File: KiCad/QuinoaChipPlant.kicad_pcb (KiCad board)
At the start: 2 copper layers, 22 x 97 mm, 26 parts, among them J1 POWER_SW, J2 POWER, J3 MOTOR, J4 SPEAKER, J5 NeoPixel, J6 Conn_01x04_Male, J8 Conn_01x04_Male, J9 Conn_01x01_Female, Q1 Q_NMOS_GSD, U1 SparkFun_TB6612FNG_MOTOR_DRIV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, U2 SparkFun_Pro_Micro_328U4, U3 MIC5205-3.3YM5, U4 TSPCBA-01-B2_nRF52810_module

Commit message: change to  KiCad 7 files from KiCad 5 files.
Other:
- net class Default removed

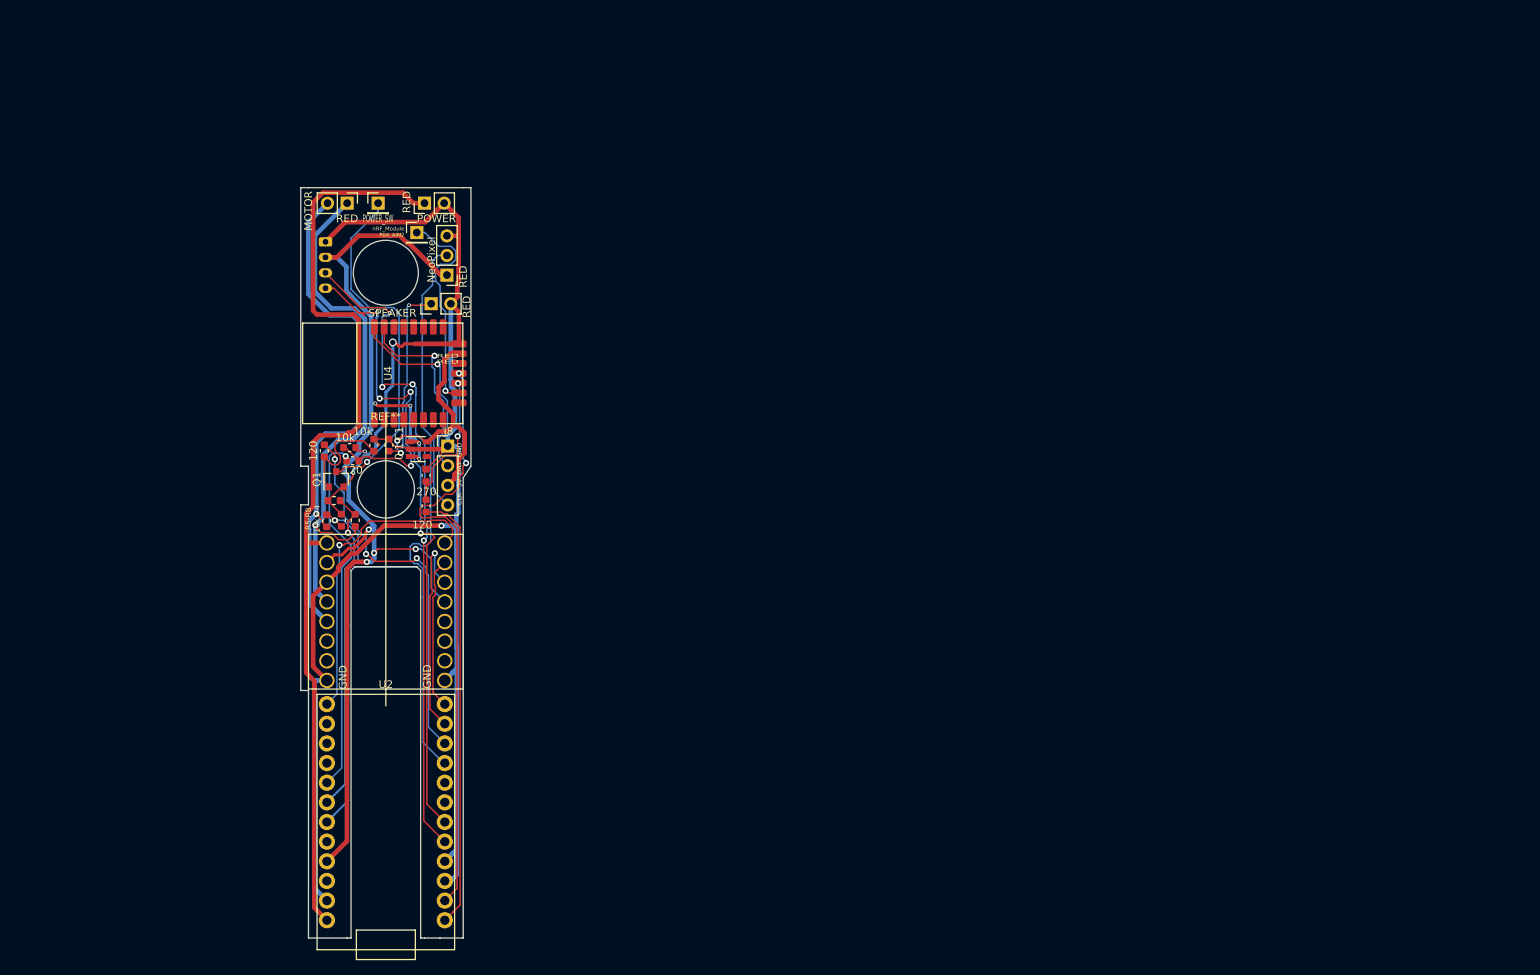
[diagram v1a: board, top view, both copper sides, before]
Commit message: make pump, bulb , sensor PCB.
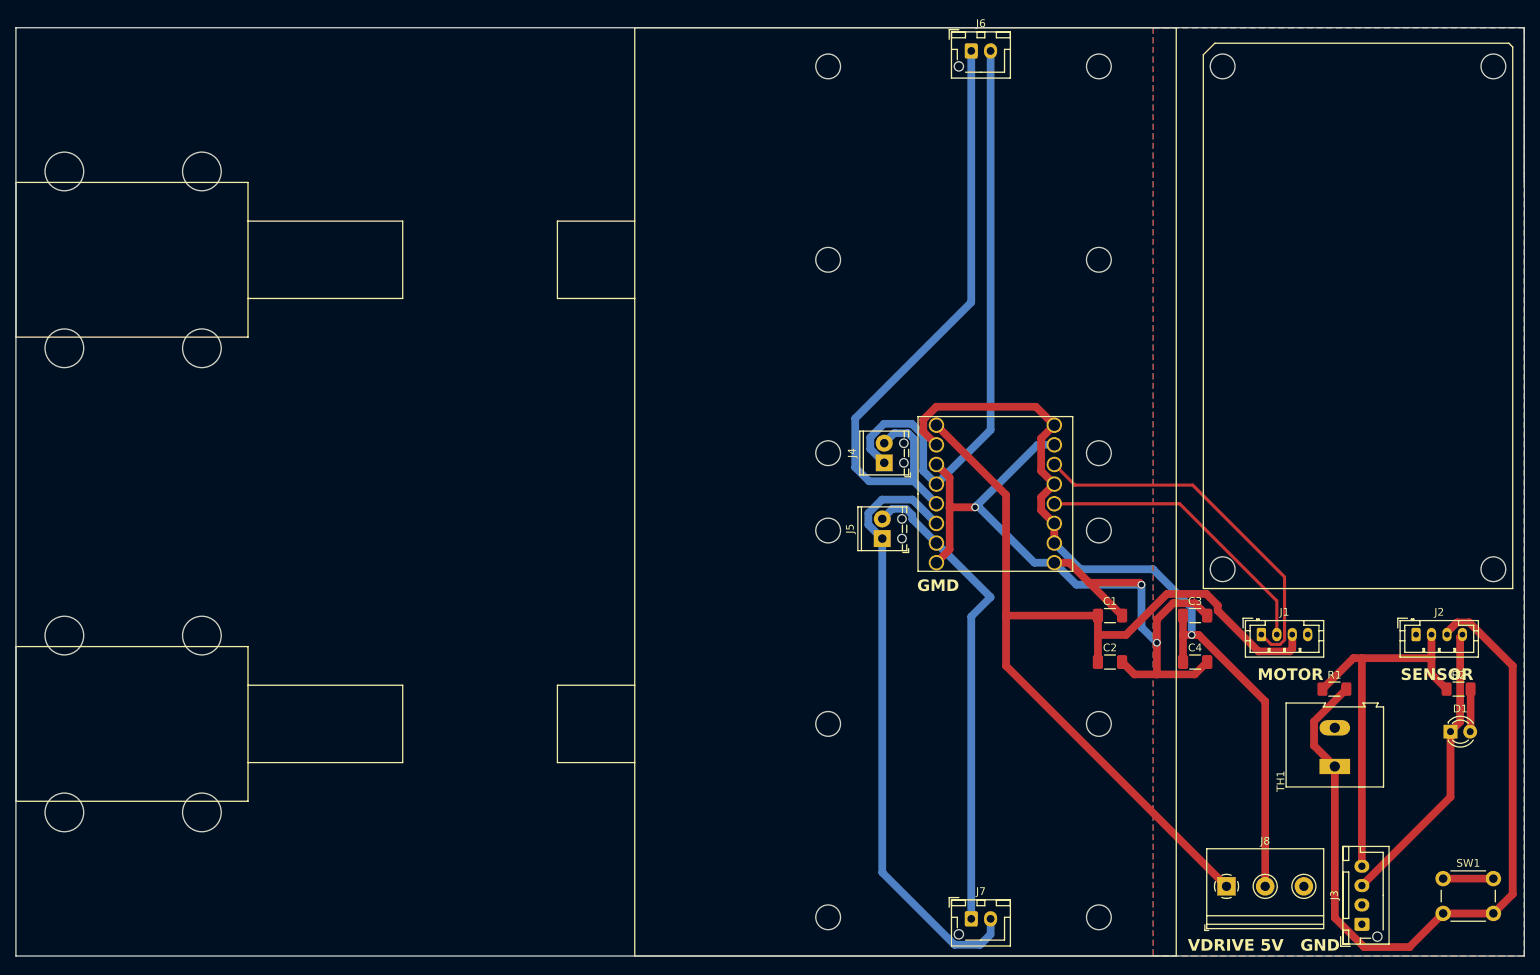
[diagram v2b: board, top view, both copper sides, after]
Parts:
- removed J9: Conn_01x01_Female, Connector_PinHeader_2.54mm:PinHeader_1x01_P2.54mm_Vertical
- removed Q1: Q_NMOS_GSD, Package_TO_SOT_SMD:SOT-23
- removed R10: 270, Resistor_SMD:R_0603_1608Metric
- removed R3, R9: 120, Resistor_SMD:R_0603_1608Metric
- removed R4, R5, R6, R7, R8: 10k, Resistor_SMD:R_0603_1608Metric
- removed the REF** at (100.0, 100.0)
- removed the REF** at (100.0, 72.0)
- removed U2: SparkFun_Pro_Micro_328U4, library:SparkFun_Pro_Micro_32U4
- removed U3: MIC5205-3.3YM5, Package_TO_SOT_SMD:SOT-23-5
- removed U4: TSPCBA-01-B2_nRF52810_module, library:TSPCBA-01-B2_nRF52810_module
- added ?: , , F.Cu at (58.4, 141.8)
- added ?: , , F.Cu at (76.2, 81.8)
- added ?: , , F.Cu at (76.2, 118.9)
- added ?: , , F.Cu at (76.2, 141.8)
- added ?: , , F.Cu at (58.4, 81.8)
- added ?: , , F.Cu at (76.2, 58.9)
- added C2: C_Polarized, Capacitor_SMD:C_1206_3216Metric_Pad1.33x1.80mm_HandSolder, F.Cu at (193.6, 122.3)
- added C3: C, Capacitor_SMD:C_1206_3216Metric_Pad1.33x1.80mm_HandSolder, F.Cu at (204.6, 116.3)
- added C4: C_Polarized, Capacitor_SMD:C_1206_3216Metric_Pad1.33x1.80mm_HandSolder, F.Cu at (204.6, 122.3)
- added D1: LED, LED_THT:LED_D3.0mm, F.Cu at (237.6, 131.3)
- added J7: BULB, Connector_JST:JST_XH_B2B-XH-AM_1x02_P2.50mm_Vertical, F.Cu at (175.7, 155.5)
- added REF**: MountingHole_3.2mm_M3, MountingHole:MountingHole_3.2mm_M3, F.Cu at (157.2, 95.3)
- added REF**: MountingHole_3.2mm_M3, MountingHole:MountingHole_3.2mm_M3, F.Cu at (192.2, 70.3)
- added REF**: MountingHole_3.2mm_M3, MountingHole:MountingHole_3.2mm_M3, F.Cu at (208.2, 45.3)
- added REF**: MountingHole_3.2mm_M3, MountingHole:MountingHole_3.2mm_M3, F.Cu at (192.2, 95.3)
- added REF**: MountingHole_3.2mm_M3, MountingHole:MountingHole_3.2mm_M3, F.Cu at (243.2, 110.3)
- added REF**: MountingHole_3.2mm_M3, MountingHole:MountingHole_3.2mm_M3, F.Cu at (243.2, 45.3)
- added REF**: MountingHole_3.2mm_M3, MountingHole:MountingHole_3.2mm_M3, F.Cu at (157.2, 155.3)
- added REF**: MountingHole_3.2mm_M3, MountingHole:MountingHole_3.2mm_M3, F.Cu at (58.4, 58.9)
- added REF**: MountingHole_3.2mm_M3, MountingHole:MountingHole_3.2mm_M3, F.Cu at (192.2, 130.3)
- added REF**: MountingHole_3.2mm_M3, MountingHole:MountingHole_3.2mm_M3, F.Cu at (208.2, 110.3)
- added REF**: MountingHole_3.2mm_M3, MountingHole:MountingHole_3.2mm_M3, F.Cu at (192.2, 105.3)
- added REF**: MountingHole_3.2mm_M3, MountingHole:MountingHole_3.2mm_M3, F.Cu at (58.4, 118.9)
- added REF**: MountingHole_3.2mm_M3, MountingHole:MountingHole_3.2mm_M3, F.Cu at (157.2, 70.3)
- added REF**: MountingHole_3.2mm_M3, MountingHole:MountingHole_3.2mm_M3, F.Cu at (192.2, 155.3)
- added REF**: MountingHole_3.2mm_M3, MountingHole:MountingHole_3.2mm_M3, F.Cu at (157.2, 105.3)
- added REF**: MountingHole_3.2mm_M3, MountingHole:MountingHole_3.2mm_M3, F.Cu at (157.2, 45.3)
- added REF**: MountingHole_3.2mm_M3, MountingHole:MountingHole_3.2mm_M3, F.Cu at (192.2, 45.3)
- added REF**: MountingHole_3.2mm_M3, MountingHole:MountingHole_3.2mm_M3, F.Cu at (157.2, 130.3)
- added SW1: SW_Push, Button_Switch_THT:SW_PUSH_6mm, F.Cu at (236.7, 150.3)
- added TH1: Thermistor, TerminalBlock:TerminalBlock_Altech_AK300-2_P5.00mm, F.Cu at (222.7, 135.8)
- C1: value 0.1 -> C; footprint Capacitor_SMD:C_0603_1608Metric -> Capacitor_SMD:C_1206_3216Metric_Pad1.33x1.80mm_HandSolder
- J1: value POWER_SW -> GROVE; footprint Connector_PinHeader_2.54mm:PinHeader_1x01_P2.54mm_Vertical -> Connector_JST:JST_PH_B4B-PH-K_1x04_P2.00mm_Vertical
- J2: value POWER -> GROVE; footprint Connector_PinHeader_2.54mm:PinHeader_1x02_P2.54mm_Vertical -> Connector_JST:JST_PH_B4B-PH-K_1x04_P2.00mm_Vertical
- J3: value MOTOR -> LEVEL; footprint Connector_PinHeader_2.54mm:PinHeader_1x02_P2.54mm_Vertical -> Connector_JST:JST_XH_B4B-XH-AM_1x04_P2.50mm_Vertical
- J4: value SPEAKER -> MOTOR; footprint Connector_PinHeader_2.54mm:PinHeader_1x02_P2.54mm_Vertical -> TerminalBlock_Phoenix:TerminalBlock_Phoenix_MPT-0,5-2-2.54_1x02_P2.54mm_Horizontal
- J5: value NeoPixel -> MOTOR; footprint Connector_PinHeader_2.54mm:PinHeader_1x03_P2.54mm_Vertical -> TerminalBlock_Phoenix:TerminalBlock_Phoenix_MPT-0,5-2-2.54_1x02_P2.54mm_Horizontal
- J6: value Conn_01x04_Male -> BULB; footprint Connector_JST:JST_PH_B4B-PH-K_1x04_P2.00mm_Vertical -> Connector_JST:JST_XH_B2B-XH-AM_1x02_P2.50mm_Vertical; moved to F.Cu
- J8: value Conn_01x04_Male -> Screw_Terminal_01x03; footprint Connector_PinHeader_2.54mm:PinHeader_1x04_P2.54mm_Vertical -> TerminalBlock_Philmore:TerminalBlock_Philmore_TB133_1x03_P5.00mm_Horizontal
- R1: value 120 -> R; footprint Resistor_SMD:R_0603_1608Metric -> Resistor_SMD:R_1206_3216Metric_Pad1.30x1.75mm_HandSolder
- R2: value 10k -> R; footprint Resistor_SMD:R_0603_1608Metric -> Resistor_SMD:R_1206_3216Metric_Pad1.30x1.75mm_HandSolder
- moved J3 160.9 mm to (226.2, 156.2), turned to 90 degrees
- moved R2 143.7 mm to (238.7, 125.8), turned to 0 degrees
- moved J2 139.8 mm to (233.2, 118.8), turned to 0 degrees
- moved R1 134.2 mm to (222.6, 125.8), turned to 0 degrees
- moved J1 127.1 mm to (213.2, 118.8)
- moved J8 115.7 mm to (208.7, 151.3)
- moved C1 95.8 mm to (193.6, 116.3), turned to 0 degrees
- moved J6 87.1 mm to (175.7, 43.3), turned to 0 degrees
- moved U1 80.3 mm to (178.8, 100.6)
- moved J5 65.8 mm to (164.2, 106.4), turned to 90 degrees
- moved J4 62.1 mm to (164.4, 96.6)
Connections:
- C1 pad 1: +3V3 -> Vdrive
- J1 pad 1: Net-(J1-Pad1) -> Net-(J1-Pin_1)
- J2 pad 1: Vdrive -> GND
- J2 pad 2: GND -> +5V
- J3 pad 1: Net-(J3-Pad1) -> unconnected-(J3-Pin_1-Pad1)
- J3 pad 2: Net-(J3-Pad2) -> GND
- J4 pad 1: Net-(J4-Pad1) -> Net-(J4-Pin_1)
- J4 pad 2: GND -> Net-(J4-Pin_2)
- J5 pad 1: +5V -> Net-(J5-Pin_1)
- J5 pad 2: Net-(J5-Pad2) -> Net-(J5-Pin_2)
- J6 pad 1: GND -> Net-(J4-Pin_2)
- J6 pad 2: +5V -> Net-(J4-Pin_1)
- J8 pad 1: GND -> Vdrive
- J8 pad 2: Net-(J8-Pad2) -> +5V
- J8 pad 3: +3V3 -> GND
- R1 pad 1: Net-(R1-Pad1) -> +5V
- R1 pad 2: Net-(Q1-Pad1) -> Net-(J2-Pin_3)
- R2 pad 1: Net-(Q1-Pad1) -> +5V
- R2 pad 2: GND -> Net-(D1-A)
- U1 pad 10: Net-(U1-Pad10) -> +5V
- U1 pad 11: Net-(U1-Pad11) -> +5V
- U1 pad 12: Net-(U1-Pad12) -> Net-(J1-Pin_2)
- U1 pad 14: Net-(U1-Pad14) -> Net-(J1-Pin_1)
- U1 pad 15: Net-(U1-Pad15) -> GND
- U1 pad 16: Net-(U1-Pad16) -> +5V
- U1 pad 4: Net-(J3-Pad1) -> Net-(J4-Pin_1)
- U1 pad 5: Net-(J3-Pad2) -> Net-(J4-Pin_2)
- U1 pad 6: Net-(U1-Pad6) -> Net-(J5-Pin_1)
- U1 pad 7: Net-(U1-Pad7) -> Net-(J5-Pin_2)
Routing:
- net GND: track 243.0 -> 117.2 mm, vias 4 -> 3
- net Net-(J2-Pin_3): track 0.00 -> 101.2 mm
- net Net-(J6-Pad3): track 86.2 -> 0.00 mm, vias 4 -> 0
- net Net-(J6-Pad4): track 85.9 -> 0.00 mm, vias 4 -> 0
- net Net-(J4-Pin_2): track 0.00 -> 82.7 mm
- net Net-(J5-Pin_1): track 0.00 -> 78.4 mm
- net Net-(J4-Pin_1): track 0.00 -> 78.1 mm
- net Net-(J7-Pad3): track 77.4 -> 0.00 mm, vias 2 -> 0
- net Net-(J5-Pad2): track 72.9 -> 0.00 mm
- net Net-(J3-Pad1): track 70.3 -> 0.00 mm, vias 1 -> 0
- net Net-(J3-Pad2): track 67.4 -> 0.00 mm, vias 1 -> 0
- net Net-(J5-Pin_2): track 0.00 -> 62.2 mm
- net Net-(J7-Pad2): track 56.9 -> 0.00 mm
- net Net-(R1-Pad1): track 49.1 -> 0.00 mm, vias 3 -> 0
- net Net-(R3-Pad1): track 47.8 -> 0.00 mm, vias 1 -> 0
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- added copper zone on F.Cu, net +5V
- added copper zone on B.Cu, net GND
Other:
- board size 22 x 97 mm -> 195 x 120 mm
- board text added: "GMD"
- board text added: "MOTOR"
- board text added: "SENSOR"
- board text added: "VDRIVE 5V GND"
- board text removed: "CLK 5V DAT GND"
- board text removed: "GND"
- board text removed: "GROVE I2C"
- board text removed: "IoTHandyFan 20190830"
- board text removed: "Pro Micro 5V 32U4 Module"
- board text removed: "R5-R8 10k x 4"
- board text removed: "RED"
- board text removed: "TB6612FNG MOTOR DRIVER MODULE"
- board text removed: "nRF_Module P04_AIN2"

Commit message: PCB release 20230510 Version.
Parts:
- added REF**: OSHW-Logo2_9.8x8mm_SilkScreen, Symbol:OSHW-Logo2_9.8x8mm_SilkScreen, F.Cu at (72.0, 155.0)
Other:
- board text added: "+ -"
- board text added: "5V"
- board text added: "5V Cx2"
- board text added: "AKBONE2020"
- board text added: "GND"
- board text added: "MOTOR DRIVER"
- board text added: "QuinoaChipPlant Water Control Ver.20230510 https://github.com/nanbuwks/QuinoaChipPlant"
- board text added: "VDRIVE"
- board text added: "VDRIVE Cx2"
- board text removed: "GMD"

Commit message: 202305 version
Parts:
- removed ? (x6): , 
- removed the J4 at (164.4, 96.6)
- removed the REF** at (208.2, 45.3)
- removed the REF** at (243.2, 110.3)
- removed the REF** at (243.2, 45.3)
- removed the REF** at (208.2, 110.3)
- removed the REF** at (58.4, 118.9)
- added BZ1: Buzzer, Buzzer_Beeper:Buzzer_12x9.5RM7.6, F.Cu at (270.6, 207.5)
- added C10: C, Capacitor_THT:CP_Radial_D5.0mm_P2.00mm, F.Cu at (215.0, 99.0)
- added C11: C, Capacitor_THT:CP_Radial_D5.0mm_P2.00mm, F.Cu at (225.0, 99.0)
- added C5: 0.1uF, Capacitor_SMD:C_1206_3216Metric_Pad1.33x1.80mm_HandSolder, F.Cu at (269.7, 103.4)
- added C6: C, Capacitor_THT:CP_Radial_D5.0mm_P2.00mm, F.Cu at (205.5, 158.4)
- added C7: C, Capacitor_THT:CP_Radial_D5.0mm_P2.00mm, F.Cu at (205.0, 177.5)
- added C8: C, Capacitor_THT:CP_Radial_D5.0mm_P2.00mm, F.Cu at (195.0, 99.0)
- added C9: C, Capacitor_THT:CP_Radial_D5.0mm_P2.00mm, F.Cu at (205.0, 99.0)
- added D2: D, Diode_THT:D_DO-41_SOD81_P5.08mm_Vertical_KathodeUp, F.Cu at (206.8, 163.5)
- added D3: D, Diode_THT:D_DO-41_SOD81_P5.08mm_Vertical_KathodeUp, F.Cu at (206.5, 182.0)
- added D4: D, Diode_THT:D_DO-41_SOD81_P5.08mm_Vertical_KathodeUp, F.Cu at (196.5, 103.9)
- added D5: D, Diode_THT:D_DO-41_SOD81_P5.08mm_Vertical_KathodeUp, F.Cu at (206.3, 103.8)
- added D6: D, Diode_THT:D_DO-41_SOD81_P5.08mm_Vertical_KathodeUp, F.Cu at (216.5, 103.9)
- added D7: D, Diode_THT:D_DO-41_SOD81_P5.08mm_Vertical_KathodeUp, F.Cu at (226.2, 103.9)
- added J10: BULB, Connector_JST:JST_XH_B2B-XH-AM_1x02_P2.50mm_Vertical, F.Cu at (202.4, 108.9)
- added J11: LEVEL2, Connector_JST:JST_XH_B4B-XH-AM_1x04_P2.50mm_Vertical, F.Cu at (231.9, 75.0)
- added J12: LEVEL3, Connector_JST:JST_XH_B4B-XH-AM_1x04_P2.50mm_Vertical, F.Cu at (231.9, 85.0)
- added J13: LEVEL4, Connector_JST:JST_XH_B4B-XH-AM_1x04_P2.50mm_Vertical, F.Cu at (231.9, 96.0)
- added J15: BULB, Connector_JST:JST_XH_B2B-XH-AM_1x02_P2.50mm_Vertical, F.Cu at (212.5, 108.9)
- added J16: BULB, Connector_JST:JST_XH_B2B-XH-AM_1x02_P2.50mm_Vertical, F.Cu at (222.5, 108.9)
- added J18: GROVE, Connector_JST:JST_PH_B4B-PH-K_1x04_P2.00mm_Vertical, F.Cu at (275.5, 86.7)
- added J6: MOTOR, Connector_JST:JST_XH_B2B-XH-AM_1x02_P2.50mm_Vertical, F.Cu at (216.4, 231.0)
- added J9: BULB, Connector_JST:JST_XH_B2B-XH-AM_1x02_P2.50mm_Vertical, F.Cu at (192.5, 108.9)
- added JP1: SolderJumper_2_Bridged, Jumper:SolderJumper-2_P1.3mm_Bridged_Pad1.0x1.5mm, F.Cu at (277.4, 123.8)
- added R10: 10K, Resistor_SMD:R_1206_3216Metric_Pad1.30x1.75mm_HandSolder, F.Cu at (254.9, 90.5)
- added R3: 470, Resistor_SMD:R_1206_3216Metric_Pad1.30x1.75mm_HandSolder, F.Cu at (257.5, 105.2)
- added R4: 470, Resistor_SMD:R_1206_3216Metric_Pad1.30x1.75mm_HandSolder, F.Cu at (257.4, 109.2)
- added R5: 470, Resistor_SMD:R_1206_3216Metric_Pad1.30x1.75mm_HandSolder, F.Cu at (257.4, 113.0)
- added R6: 470, Resistor_SMD:R_1206_3216Metric_Pad1.30x1.75mm_HandSolder, F.Cu at (257.4, 116.8)
- added R7: 10K, Resistor_SMD:R_1206_3216Metric_Pad1.30x1.75mm_HandSolder, F.Cu at (247.2, 85.7)
- added R8: 10K, Resistor_SMD:R_1206_3216Metric_Pad1.30x1.75mm_HandSolder, F.Cu at (254.9, 85.7)
- added R9: 10K, Resistor_SMD:R_1206_3216Metric_Pad1.30x1.75mm_HandSolder, F.Cu at (247.2, 90.2)
- added REF**: MountingHole_3.2mm_M3, MountingHole:MountingHole_3.2mm_M3, F.Cu at (109.1, 109.0)
- added REF**: MountingHole_3.2mm_M3, MountingHole:MountingHole_3.2mm_M3, F.Cu at (140.9, 169.8)
- added REF**: MountingHole_3.2mm_M3, MountingHole:MountingHole_3.2mm_M3, F.Cu at (121.8, 135.2)
- added REF**: MountingHole_3.2mm_M3, MountingHole:MountingHole_3.2mm_M3, F.Cu at (158.6, 94.2)
- added REF**: MountingHole_3.2mm_M3, MountingHole:MountingHole_3.2mm_M3, F.Cu at (149.1, 109.0)
- added REF**: MountingHole_3.2mm_M3, MountingHole:MountingHole_3.2mm_M3, F.Cu at (178.6, 109.0)
- added REF**: MountingHole_3.2mm_M3, MountingHole:MountingHole_3.2mm_M3, F.Cu at (193.2, 65.2)
- added REF**: MountingHole_3.2mm_M3, MountingHole:MountingHole_3.2mm_M3, F.Cu at (140.9, 183.8)
- added REF**: MountingHole_3.2mm_M3, MountingHole:MountingHole_3.2mm_M3, F.Cu at (103.5, 232.0)
- added REF**: MountingHole_3.2mm_M3, MountingHole:MountingHole_3.2mm_M3, F.Cu at (129.1, 94.2)
- added REF**: MountingHole_3.2mm_M3, MountingHole:MountingHole_3.2mm_M3, F.Cu at (193.2, 79.2)
- added REF**: MountingHole_3.2mm_M3, MountingHole:MountingHole_3.2mm_M3, F.Cu at (291.4, 232.0)
- added REF**: MountingHole_3.2mm_M3, MountingHole:MountingHole_3.2mm_M3, F.Cu at (121.8, 144.7)
- added REF**: MountingHole_3.2mm_M3, MountingHole:MountingHole_3.2mm_M3, F.Cu at (138.6, 109.0)
- added REF**: MountingHole_3.2mm_M3, MountingHole:MountingHole_3.2mm_M3, F.Cu at (103.5, 62.8)
- added REF**: MountingHole_3.2mm_M3, MountingHole:MountingHole_3.2mm_M3, F.Cu at (169.1, 94.2)
- added REF**: MountingHole_3.2mm_M3, MountingHole:MountingHole_3.2mm_M3, F.Cu at (207.4, 65.5)
- added REF**: MountingHole_3.2mm_M3, MountingHole:MountingHole_3.2mm_M3, F.Cu at (155.2, 170.0)
- added REF**: MountingHole_3.2mm_M3, MountingHole:MountingHole_3.2mm_M3, F.Cu at (129.1, 109.0)
- added REF**: MountingHole_3.2mm_M3, MountingHole:MountingHole_3.2mm_M3, F.Cu at (207.4, 79.5)
- added REF**: MountingHole_3.2mm_M3, MountingHole:MountingHole_3.2mm_M3, F.Cu at (290.9, 62.8)
- added REF**: MountingHole_3.2mm_M3, MountingHole:MountingHole_3.2mm_M3, F.Cu at (107.0, 144.7)
- added REF**: MountingHole_3.2mm_M3, MountingHole:MountingHole_3.2mm_M3, F.Cu at (121.8, 215.2)
- added REF**: MountingHole_3.2mm_M3, MountingHole:MountingHole_3.2mm_M3, F.Cu at (121.8, 205.7)
- added REF**: MountingHole_3.2mm_M3, MountingHole:MountingHole_3.2mm_M3, F.Cu at (149.1, 94.2)
- added REF**: MountingHole_3.2mm_M3, MountingHole:MountingHole_3.2mm_M3, F.Cu at (118.6, 109.0)
- added REF**: MountingHole_3.2mm_M3, MountingHole:MountingHole_3.2mm_M3, F.Cu at (107.0, 205.7)
- added REF**: MountingHole_3.2mm_M3, MountingHole:MountingHole_3.2mm_M3, F.Cu at (169.1, 109.0)
- added REF**: MountingHole_3.2mm_M3, MountingHole:MountingHole_3.2mm_M3, F.Cu at (138.6, 94.2)
- added REF**: MountingHole_3.2mm_M3, MountingHole:MountingHole_3.2mm_M3, F.Cu at (155.2, 184.0)
- added REF**: MountingHole_3.2mm_M3, MountingHole:MountingHole_3.2mm_M3, F.Cu at (107.0, 215.2)
- added REF**: MountingHole_3.2mm_M3, MountingHole:MountingHole_3.2mm_M3, F.Cu at (118.6, 94.2)
- added REF**: MountingHole_3.2mm_M3, MountingHole:MountingHole_3.2mm_M3, F.Cu at (158.6, 109.0)
- added REF**: MountingHole_3.2mm_M3, MountingHole:MountingHole_3.2mm_M3, F.Cu at (178.6, 94.2)
- added REF**: MountingHole_3.2mm_M3, MountingHole:MountingHole_3.2mm_M3, F.Cu at (109.1, 94.2)
- added U1: ESP32_DEVKIT_V1, library:ESP32_DEVKIT_V1, F.Cu at (272.8, 83.0)
- added U3: SparkFun_TB6612FNG_MOTOR_DRIVER_MODULE, library:SparkFun_TB6612FNG_MOTOR_DRIVER_MODULE, F.Cu at (251.4, 175.6)
- added U4: SparkFun_TB6612FNG_MOTOR_DRIVER_MODULE, library:SparkFun_TB6612FNG_MOTOR_DRIVER_MODULE, F.Cu at (278.9, 175.5)
- added U5: SEEED_GROVE, library:Seeedstudio_Grove_110990030_Vertical_4pin_2mmpitch, F.Cu at (244.9, 110.0)
- added U7: CR2013-MI2120, library:TFT3.2_ILI9341, F.Cu at (220.0, 200.0)
- added USB Cable: MountingHole_8.4mm_M8, MountingHole:MountingHole_8.4mm_M8, F.Cu at (279.4, 140.0)
- C2, C4: footprint Capacitor_SMD:C_1206_3216Metric_Pad1.33x1.80mm_HandSolder -> Capacitor_THT:CP_Radial_D10.0mm_P2.50mm_P5.00mm
- J2: value GROVE -> DCJACK; footprint Connector_JST:JST_PH_B4B-PH-K_1x04_P2.00mm_Vertical -> library:DCJACK
- J3: value LEVEL -> LEVEL1
- J5: footprint TerminalBlock_Phoenix:TerminalBlock_Phoenix_MPT-0,5-2-2.54_1x02_P2.54mm_Horizontal -> Connector_JST:JST_XH_B2B-XH-AM_1x02_P2.50mm_Vertical
- R2: value R -> 470
- moved J7 128.1 mm to (203.0, 168.4)
- moved J3 91.9 mm to (231.9, 64.5), turned to 0 degrees
- moved REF** 90.4 mm to (107.0, 135.2)
- moved D1 90.2 mm to (285.9, 207.5)
- moved REF** 86.0 mm to (112.2, 231.0)
- moved REF** 85.7 mm to (232.6, 230.8)
- moved REF** 85.7 mm to (232.6, 120.8)
- moved REF** 85.7 mm to (232.6, 145.8)
- moved REF** 85.7 mm to (232.6, 170.8)
- moved REF** 85.7 mm to (232.6, 205.8)
- moved REF** 85.7 mm to (232.6, 180.8)
- moved U2 85.6 mm to (219.1, 176.1)
- moved REF** 83.4 mm to (192.6, 145.8)
- moved REF** 83.4 mm to (192.6, 180.8)
- moved REF** 83.4 mm to (192.6, 120.8)
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- renumbered J8 to J4, J6 to J7, J7 to J8, U1 to U2
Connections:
- net Net-(J1-Pin_1) renamed MOTOR1
- net Net-(J1-Pin_2) renamed MOTOR2
- D1 pad 1: Net-(D1-K) -> WATERSENSOR1
- J2 pad 1: GND -> +5V
- J2 pad 2: +5V -> GND
- J2 pad 3: Net-(J2-Pin_3) -> GND
- J3 pad 1: unconnected-(J3-Pin_1-Pad1) -> GND
- J3 pad 3: Net-(D1-K) -> Net-(J3-Pin_3)
- J3 pad 4: +5V -> WATERSENSOR1
- J5 pad 1: Net-(J5-Pin_1) -> Net-(D2-K)
- J5 pad 2: Net-(J5-Pin_2) -> Net-(D2-A)
- J7 pad 1: Net-(J4-Pin_2) -> Net-(D2-A)
- J7 pad 2: Net-(J4-Pin_1) -> Net-(D2-K)
- J8 pad 1: Net-(J5-Pin_2) -> Net-(D3-A)
- J8 pad 2: Net-(J5-Pin_1) -> Net-(D3-K)
- R1 pad 1: +5V -> +3V3
- R1 pad 2: Net-(J2-Pin_3) -> SW_THERMISTOR
- R2 pad 1: +5V -> +3V3
- SW1 pad 2: Net-(J2-Pin_3) -> SW_THERMISTOR
- TH1 pad 1: Net-(J2-Pin_3) -> SW_THERMISTOR
- U2 pad 10: +5V -> +3V3
- U2 pad 11: +5V -> +3V3
- U2 pad 13: +5V -> +3V3
- U2 pad 16: +5V -> +3V3
- U2 pad 2: +5V -> +3V3
- U2 pad 4: Net-(J4-Pin_1) -> Net-(D2-K)
- U2 pad 5: Net-(J4-Pin_2) -> Net-(D2-A)
- U2 pad 6: Net-(J5-Pin_1) -> Net-(D3-A)
- U2 pad 7: Net-(J5-Pin_2) -> Net-(D3-K)
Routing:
- net +3V3: track 0.00 -> 505.2 mm, vias 0 -> 4
- net SW_THERMISTOR: track 0.00 -> 230.6 mm, vias 0 -> 5
- net WATERSENSOR1: track 0.00 -> 207.6 mm, vias 0 -> 2
- net Net-(D6-K): track 0.00 -> 180.2 mm
- net Net-(U1-23): track 0.00 -> 165.9 mm
- net Net-(U1-5): track 0.00 -> 157.4 mm
- net Net-(D6-A): track 0.00 -> 156.8 mm
- net Net-(U1-18): track 0.00 -> 156.7 mm, vias 0 -> 1
- net Net-(U1-19): track 0.00 -> 155.6 mm, vias 0 -> 1
- net Net-(U1-16): track 0.00 -> 151.7 mm, vias 0 -> 1
- net Net-(U1-17): track 0.00 -> 151.2 mm, vias 0 -> 1
- net Net-(U1-4): track 0.00 -> 150.8 mm, vias 0 -> 1
- net Net-(D4-A): track 0.00 -> 148.6 mm
- net Net-(D7-A): track 0.00 -> 147.4 mm
- net Net-(BZ1--): track 0.00 -> 140.4 mm
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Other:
- board size 195 x 120 mm -> 195.3 x 185 mm
- board text added: "Ext Control"
- board text added: "NeoPixel"
- board text added: "QuinoaChipPlant Water Control Ver.20230579 https://github.com/nanbuwks/QuinoaChipPlant"
- board text added: "VDrive 5V GND"
- board text removed: "5V"
- board text removed: "AKBONE2020"
- board text removed: "QuinoaChipPlant Water Control Ver.20230510 https://github.com/nanbuwks/QuinoaChipPlant"
